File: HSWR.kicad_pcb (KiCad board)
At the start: 4 copper layers, 152 x 139 mm, 150 parts, among them IC1 B1212S-2W, IC2 JW5052C, IC3 JW5052C, IC4 ADUM3054, IC5 ADuM4160, J1 USB_B, J2 IO, J3 B+, J4 B-, J5 U, J6 V, J7 W, J8 SWD, Q1 IXFK300N20X3, Q2 IXFK300N20X3, Q3 IXFK300N20X3, Q4 IXFK300N20X3, Q5 IXFK300N20X3, Q6 IXFK300N20X3, U1 ACS781xLRTR-150B, U2 ACS781xLRTR-150B, U3 ACS781xLRTR-150B, U4 STM32F405RGTx, U5 IRS2186, U6 IRS2186, U7 IRS2186, U8 AP1117-50, Y1 8MHz

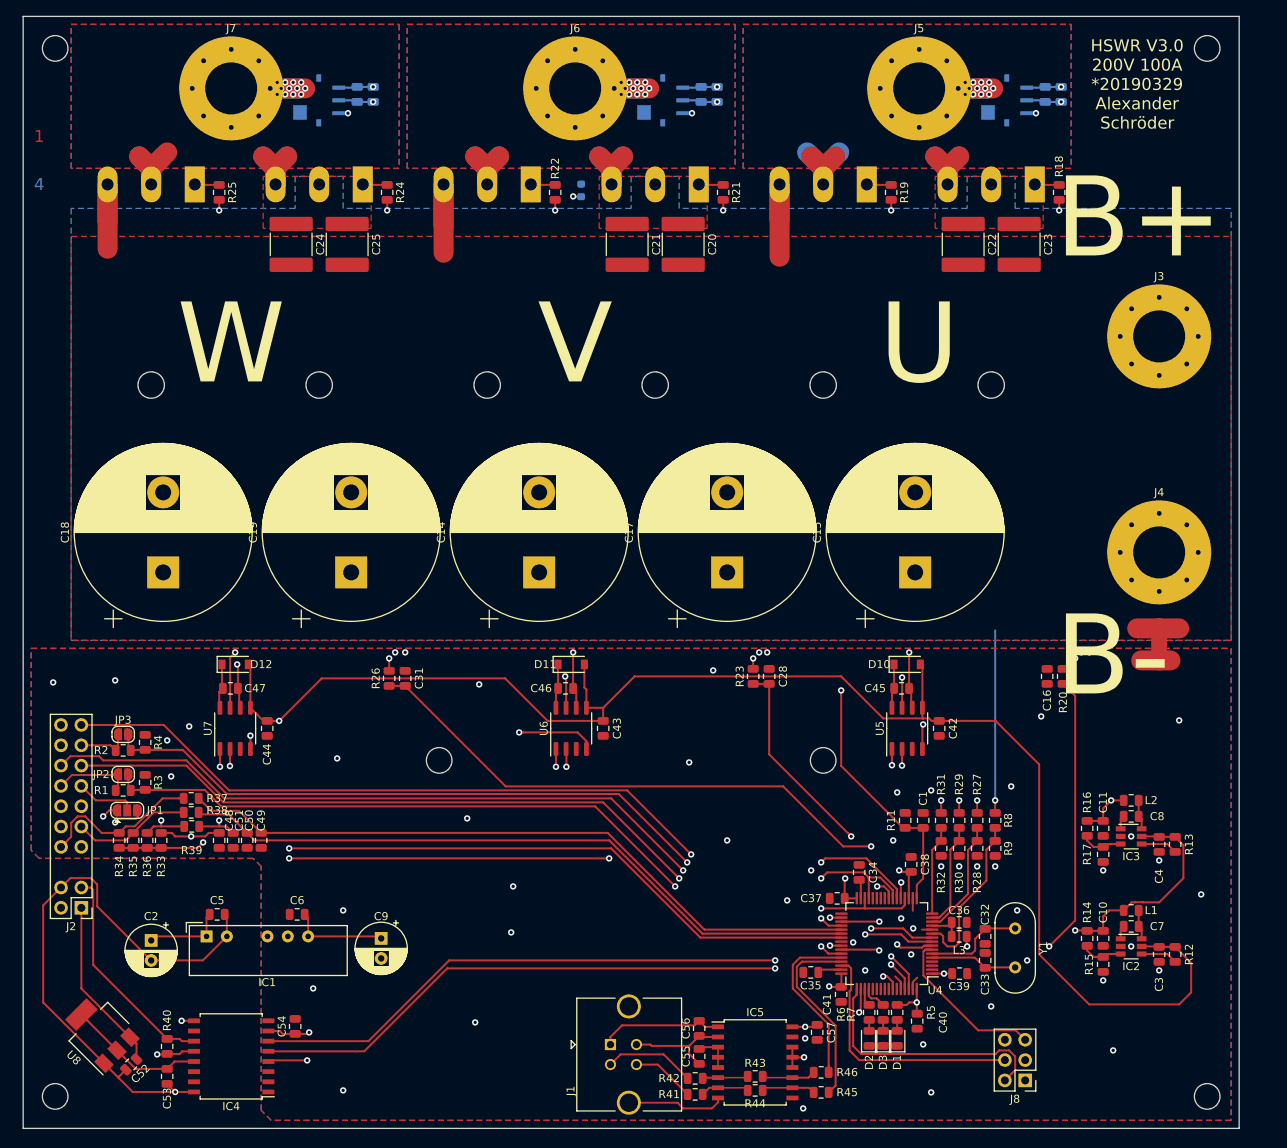
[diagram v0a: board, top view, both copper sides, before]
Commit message: - reworked IO section -> now fully isolated - added fan output - sensor IO is now differential - exposed differential UART interface - fan pin not defined yet!
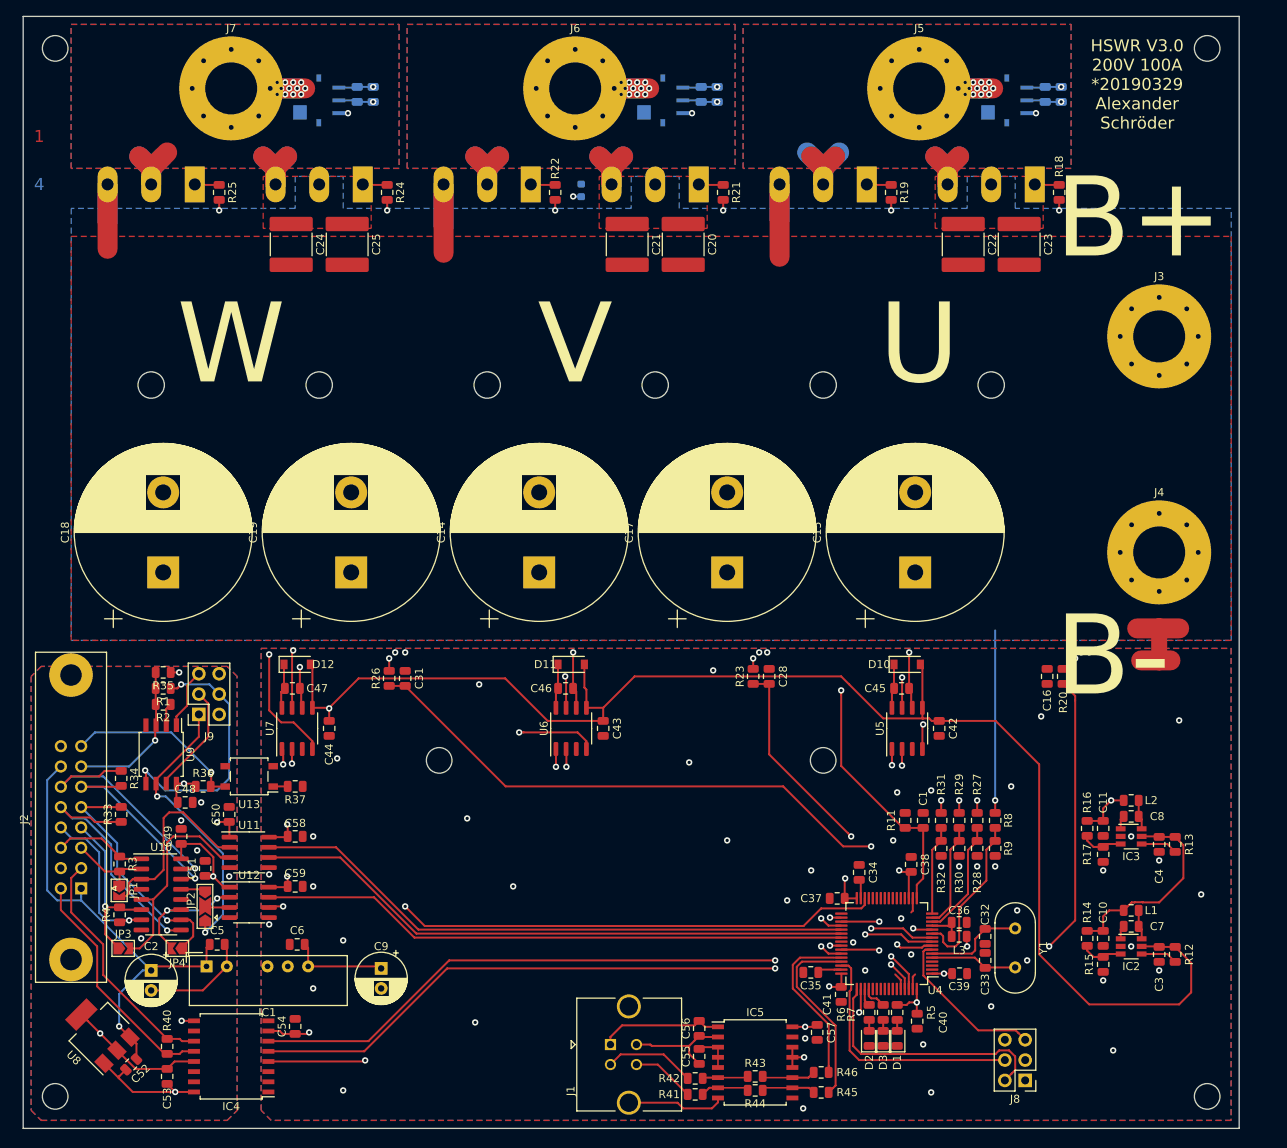
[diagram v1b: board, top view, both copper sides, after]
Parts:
- removed R38, R39: 10k, Resistor_SMD:R_0805_2012Metric
- added C58: 100n, Capacitor_SMD:C_0805_2012Metric, F.Cu at (101.0, 126.5)
- added C59: 100n, Capacitor_SMD:C_0805_2012Metric, F.Cu at (101.0, 132.8)
- added J9: AVR-ISP-6, Connector_PinSocket_2.54mm:PinSocket_2x03_P2.54mm_Vertical, F.Cu at (89.0, 111.2)
- added JP4: H3, Jumper:SolderJumper-2_P1.3mm_Open_TrianglePad1.0x1.5mm, F.Cu at (86.3, 140.5)
- added U10: AM26LV32xD, Package_SO:SOIC-16_3.9x9.9mm_P1.27mm, F.Cu at (84.2, 133.8)
- added U11: ADuM120N, Package_SO:SOIC-8_3.9x4.9mm_P1.27mm, F.Cu at (95.2, 128.5)
- added U12: ADuM120N, Package_SO:SOIC-8_3.9x4.9mm_P1.27mm, F.Cu at (95.2, 134.8)
- added U13: SFH617A-1, Package_SO:SO-4_4.4x4.3mm_P2.54mm, F.Cu at (95.2, 119.0)
- added U9: ATtiny13A-SU, Package_SO:SOIJ-8_5.3x5.3mm_P1.27mm, F.Cu at (84.2, 116.2)
- C48, C49, C50, C51: value 4n7 -> 100n
- J2: footprint Auktora:PinHeader_2x10_P2.54mm_Vertical -> Connector_IDC:IDC-Header_2x08_P2.54mm_Vertical_Lock
- JP1: value 5V/3V3 -> H1; footprint Jumper:SolderJumper-3_P1.3mm_Open_RoundedPad1.0x1.5mm -> Jumper:SolderJumper-2_P1.3mm_Open_TrianglePad1.0x1.5mm
- JP2: value opt. -> UART; footprint Jumper:SolderJumper-2_P1.3mm_Open_RoundedPad1.0x1.5mm -> Jumper:SolderJumper-3_P2.0mm_Open_TrianglePad1.0x1.5mm
- JP3: value opt. -> H2; footprint Jumper:SolderJumper-2_P1.3mm_Open_RoundedPad1.0x1.5mm -> Jumper:SolderJumper-2_P1.3mm_Open_TrianglePad1.0x1.5mm
- R1: value 1k -> 100R
- R3, R4: value 1k5 -> 120R
- R33: value 10k -> 120R
- R34: value 2k2 -> 120R
- R35: value 2k2 -> 10k
- R36: value 2k2 -> 1k
- R37: value 10k -> 100R
- moved JP3 26.8 mm to (79.5, 140.5)
- moved R4 21.8 mm to (79.0, 136.3), turned to 90 degrees
- moved R35 21.3 mm to (84.5, 106.0), turned to 180 degrees
- moved JP2 19.4 mm to (89.8, 135.2), turned to 90 degrees
- moved R1 13.7 mm to (84.5, 108.0)
- moved R37 13.1 mm to (101.0, 120.2), turned to 180 degrees
- moved R3 10.7 mm to (79.0, 129.9)
- moved JP1 10.0 mm to (79.0, 133.2), turned to 270 degrees
- moved C49 10.0 mm to (86.8, 126.5), turned to 90 degrees
- moved R36 9.72 mm to (89.5, 120.2), turned to 0 degrees
- moved R34 7.75 mm to (79.2, 119.2)
- moved C44 7.75 mm to (105.2, 113.0)
- moved C47 7.75 mm to (100.7, 108.0)
- moved D12 7.75 mm to (101.2, 105.0)
- moved U7 7.75 mm to (101.2, 113.0)
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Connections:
- C48 pad 1: /Filters/TEMP_IN -> +5VA
- C48 pad 2: GND -> Earth
- C49 pad 1: /Filters/HALL3_OUT -> +5VA
- C49 pad 2: GND -> Earth
- C50 pad 1: /Filters/HALL2_OUT -> +5VA
- C50 pad 2: GND -> Earth
- C51 pad 1: /Filters/HALL1_OUT -> +5VA
- C51 pad 2: GND -> Earth
- C53 pad 1: Net-(C53-Pad1) -> +5VA
- IC4 pad 10: Net-(IC4-Pad10) -> (no net)
- IC4 pad 13: Net-(C53-Pad1) -> +5VA
- J2 pad 10: /Filters/HALL1_IN -> /iso IO/Hall_3B
- J2 pad 11: /Filters/TEMP_IN -> /iso IO/UART_A
- J2 pad 12: GND -> /iso IO/UART_B
- J2 pad 13: Net-(J2-Pad13) -> /iso IO/M_Temp
- J2 pad 14: Net-(J2-Pad14) -> +12VA
- J2 pad 15: /MCU/RX_SDA_NSS -> /iso IO/Fan_Out
- J2 pad 16: /MCU/TX_SCL_MOSI -> Earth
- J2 pad 7: +5V -> /iso IO/Hall_2A
- J2 pad 8: /Filters/HALL3_IN -> /iso IO/Hall_2B
- J2 pad 9: /Filters/HALL2_IN -> /iso IO/Hall_3A
- J8 pad 6: Net-(J8-Pad6) -> (no net)
- JP1 pad 1: +3V3 -> /iso IO/Hall_1A
- JP1 pad 2: Net-(J2-Pad13) -> Net-(JP1-Pad2)
- JP2 pad 1: Net-(J2-Pad14) -> Net-(J9-Pad1)
- JP2 pad 2: /MCU/SCK_ADC_EXT -> Net-(JP2-Pad2)
- JP3 pad 1: Net-(J2-Pad17) -> /iso IO/Hall_2A
- JP3 pad 2: /MCU/MISO_ADC_EXT2 -> Net-(JP3-Pad2)
- R1 pad 1: /MCU/SCK_ADC_EXT -> Net-(J9-Pad4)
- R1 pad 2: Net-(J2-Pad14) -> /iso IO/M_Temp
- R2 pad 1: /MCU/MISO_ADC_EXT2 -> Net-(R2-Pad1)
- R2 pad 2: Net-(J2-Pad17) -> /iso IO/M_Temp
- R3 pad 1: GND -> /iso IO/Hall_1B
- R3 pad 2: /MCU/SCK_ADC_EXT -> /iso IO/Hall_1A
- R33 pad 1: /Filters/TEMP_IN -> /iso IO/Hall_3B
- R33 pad 2: +3V3 -> /iso IO/Hall_3A
- R34 pad 1: /Filters/HALL3_IN -> /iso IO/UART_B
- R34 pad 2: +3V3 -> /iso IO/UART_A
- R35 pad 1: /Filters/HALL2_IN -> +5VA
- R35 pad 2: +3V3 -> /iso IO/M_Temp
- R36 pad 1: /Filters/HALL1_IN -> +5VA
- R36 pad 2: +3V3 -> /iso IO/Fan_Out
- R37 pad 1: /Filters/HALL3_IN -> (no net)
- R37 pad 2: /Filters/HALL3_OUT -> Net-(R37-Pad2)
- R4 pad 1: GND -> /iso IO/Hall_2B
- R4 pad 2: /MCU/MISO_ADC_EXT2 -> /iso IO/Hall_2A
- U1 pad 4: Net-(U1-Pad4) -> (no net)
- U1 pad 7: Net-(U1-Pad7) -> (no net)
- U2 pad 4: Net-(U2-Pad4) -> (no net)
- U2 pad 7: Net-(U2-Pad7) -> (no net)
- U3 pad 4: Net-(U3-Pad4) -> (no net)
- U3 pad 7: Net-(U3-Pad7) -> (no net)
- U4 pad 2: Net-(U4-Pad2) -> (no net)
- U4 pad 20: /MCU/RX_SDA_NSS -> (no net)
- U4 pad 21: /MCU/SCK_ADC_EXT -> (no net)
- U4 pad 22: /MCU/MISO_ADC_EXT2 -> (no net)
- U4 pad 23: /MCU/TX_SCL_MOSI -> (no net)
- U4 pad 24: /Filters/TEMP_IN -> (no net)
- U4 pad 25: Net-(U4-Pad25) -> (no net)
- U4 pad 26: Net-(U4-Pad26) -> (no net)
- U4 pad 27: Net-(U4-Pad27) -> (no net)
- U4 pad 28: Net-(U4-Pad28) -> (no net)
- U4 pad 29: /MCU/TX_SCL_MOSI -> (no net)
- U4 pad 3: Net-(U4-Pad3) -> (no net)
- U4 pad 30: /MCU/RX_SDA_NSS -> /iso IO/UART
- U4 pad 33: Net-(U4-Pad33) -> (no net)
- U4 pad 37: /Filters/HALL3_OUT -> /MCU/HALL_1
- U4 pad 38: /Filters/HALL2_OUT -> /MCU/HALL_2
- U4 pad 39: /Filters/HALL1_OUT -> /MCU/HALL_3
- U4 pad 4: Net-(U4-Pad4) -> (no net)
- U4 pad 40: Net-(U4-Pad40) -> (no net)
- U4 pad 53: Net-(U4-Pad53) -> (no net)
- U4 pad 54: Net-(U4-Pad54) -> (no net)
- U4 pad 55: Net-(U4-Pad55) -> (no net)
- U4 pad 56: Net-(U4-Pad56) -> (no net)
- U4 pad 57: Net-(U4-Pad57) -> (no net)
- U4 pad 58: /MCU/SERVO -> (no net)
- U4 pad 59: Net-(U4-Pad59) -> (no net)
- U8 pad 2: Net-(C53-Pad1) -> +5VA
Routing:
- net +5V: track 177.0 -> 25.6 mm, vias 2 -> 0
- net /MCU/SERVO: track 122.3 -> 0.00 mm, vias 2 -> 0
- net /Filters/TEMP_IN: track 117.5 -> 0.00 mm, vias 4 -> 0
- net /MCU/TX_SCL_MOSI: track 115.6 -> 0.00 mm, vias 2 -> 0
- net /MCU/RX_SDA_NSS: track 112.7 -> 0.00 mm, vias 2 -> 0
- net /MCU/MISO_ADC_EXT2: track 106.7 -> 0.00 mm, vias 2 -> 0
- net /MCU/SCK_ADC_EXT: track 106.3 -> 0.00 mm, vias 2 -> 0
- net /Filters/HALL1_OUT: track 89.2 -> 0.00 mm, vias 2 -> 0
- net /Filters/HALL3_OUT: track 87.1 -> 0.00 mm
- net /Filters/HALL2_OUT: track 86.6 -> 0.00 mm
- net /iso IO/UART: track 0.00 -> 77.5 mm, vias 0 -> 2
- net /MCU/HALL_1: track 0.00 -> 75.8 mm
- net /MCU/HALL_2: track 0.00 -> 75.5 mm
- net /MCU/HALL_3: track 0.00 -> 73.6 mm
- net Earth: track 83.5 -> 39.9 mm, vias 2 -> 7
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- added copper zone on GND, net +12VA
- added copper zone on Power1, net +5VA
- added copper zone on B.Cu, net Earth
- added copper zone on F.Cu, net Earth

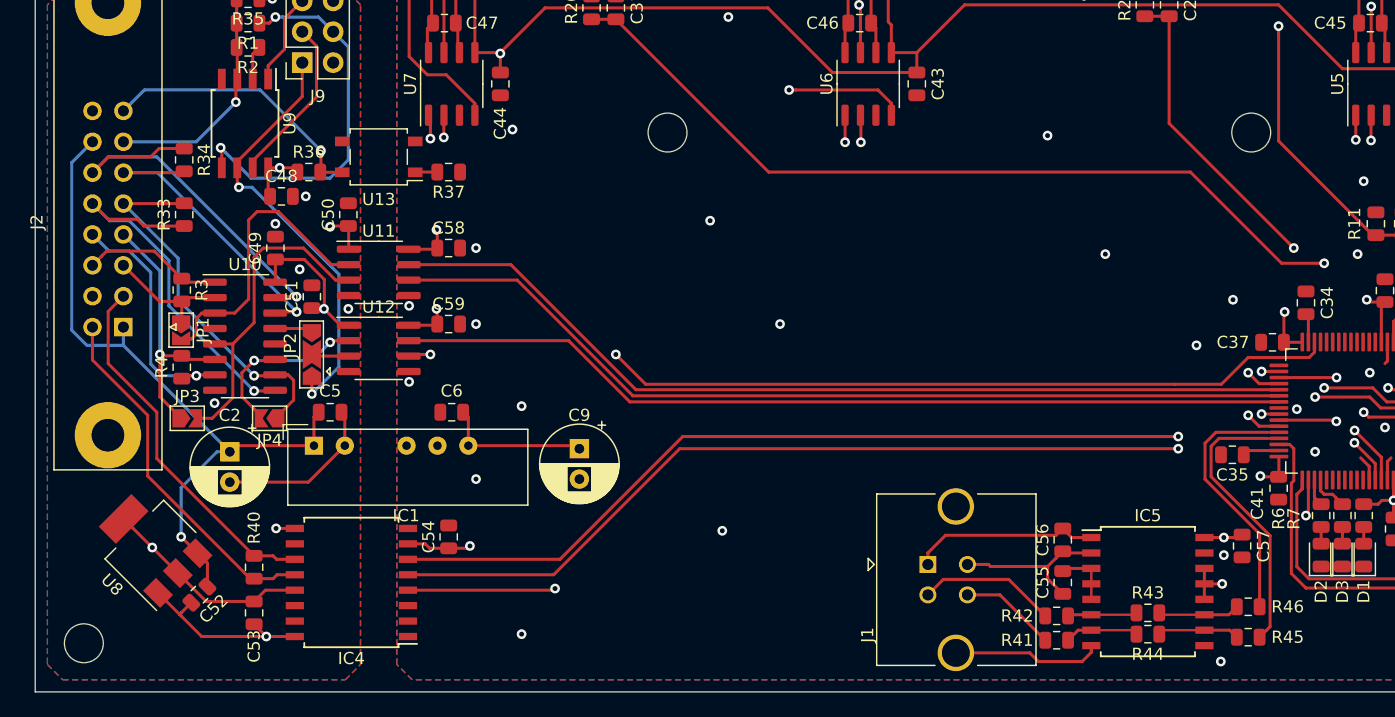
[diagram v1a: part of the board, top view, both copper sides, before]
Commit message: - added high power capabilities to fan output - moved CAN isolator - connected fan output to PB10 (TIM2_CH3)
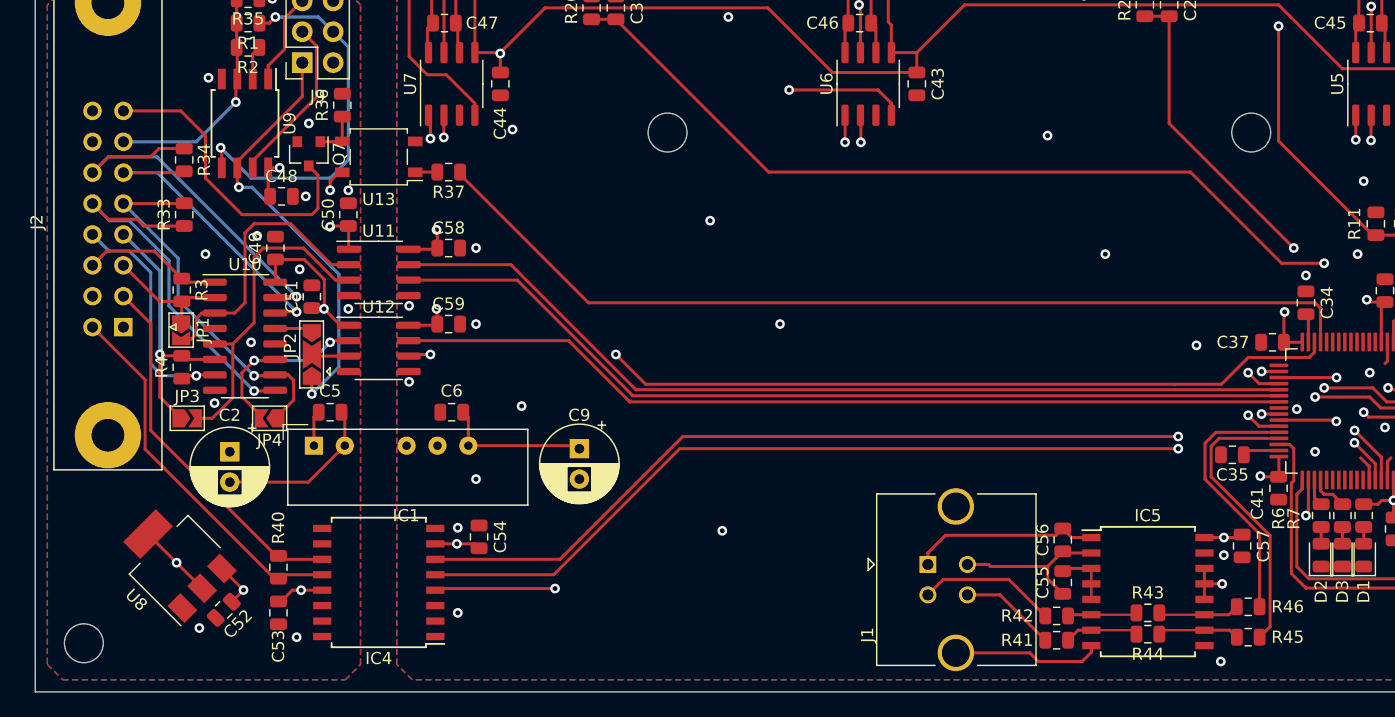
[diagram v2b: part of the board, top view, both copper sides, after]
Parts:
- added Q7: Q_NMOS_GSD, Package_TO_SOT_SMD:SOT-23, F.Cu at (89.5, 118.8)
- U13: value SFH617A-1 -> PC355
- moved R36 6.15 mm to (92.2, 114.8), turned to 90 degrees
- moved C54 2.50 mm to (103.5, 150.2)
- moved C52 2.36 mm to (82.5, 156.2)
- moved U8 2.36 mm to (78.5, 152.2)
- moved IC4 2.25 mm to (95.2, 154.0)
- moved C53 2.00 mm to (87.0, 156.5)
- moved R40 2.00 mm to (87.0, 152.8)
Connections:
- IC4 pad 10: (no net) -> Net-(IC4-Pad10)
- J8 pad 6: (no net) -> Net-(J8-Pad6)
- R36 pad 1: +5VA -> Net-(Q7-Pad1)
- R36 pad 2: /iso IO/Fan_Out -> Earth
- R37 pad 1: (no net) -> /MCU/Fan_CPU
- U1 pad 4: (no net) -> Net-(U1-Pad4)
- U1 pad 7: (no net) -> Net-(U1-Pad7)
- U10 pad 12: (no net) -> Earth
- U10 pad 4: (no net) -> Net-(U10-Pad4)
- U13 pad 3: Earth -> Net-(Q7-Pad1)
- U13 pad 4: /iso IO/Fan_Out -> +12VA
- U2 pad 4: (no net) -> Net-(U2-Pad4)
- U2 pad 7: (no net) -> Net-(U2-Pad7)
- U3 pad 4: (no net) -> Net-(U3-Pad4)
- U3 pad 7: (no net) -> Net-(U3-Pad7)
- U4 pad 2: (no net) -> Net-(U4-Pad2)
- U4 pad 20: (no net) -> Net-(U4-Pad20)
- U4 pad 21: (no net) -> Net-(U4-Pad21)
- U4 pad 22: (no net) -> Net-(U4-Pad22)
- U4 pad 23: (no net) -> Net-(U4-Pad23)
- U4 pad 24: (no net) -> Net-(U4-Pad24)
- U4 pad 25: (no net) -> Net-(U4-Pad25)
- U4 pad 26: (no net) -> Net-(U4-Pad26)
- U4 pad 27: (no net) -> Net-(U4-Pad27)
- U4 pad 28: (no net) -> Net-(U4-Pad28)
- U4 pad 29: (no net) -> /MCU/Fan_CPU
- U4 pad 3: (no net) -> Net-(U4-Pad3)
- U4 pad 33: (no net) -> Net-(U4-Pad33)
- U4 pad 4: (no net) -> Net-(U4-Pad4)
- U4 pad 40: (no net) -> Net-(U4-Pad40)
- U4 pad 53: (no net) -> Net-(U4-Pad53)
- U4 pad 54: (no net) -> Net-(U4-Pad54)
- U4 pad 55: (no net) -> Net-(U4-Pad55)
- U4 pad 56: (no net) -> Net-(U4-Pad56)
- U4 pad 57: (no net) -> Net-(U4-Pad57)
- U4 pad 58: (no net) -> Net-(U4-Pad58)
- U4 pad 59: (no net) -> Net-(U4-Pad59)
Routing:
- net /MCU/Fan_CPU: track 0.00 -> 78.3 mm
- net +12VA: track 59.1 -> 8.83 mm, vias 1 -> 2
- net Earth: track 39.9 -> 13.6 mm, vias 7 -> 12
- net +5VA: track 39.4 -> 30.8 mm, vias 5 -> 6
- net Net-(Q7-Pad1): track 0.00 -> 3.85 mm
- net /iso IO/Fan_Out: track 22.6 -> 25.6 mm, vias 1 -> 0
- net /CAN bus transceiver/CAN_TX: track 87.2 -> 85.0 mm
- net /CAN bus transceiver/CAN_RX: track 86.5 -> 84.3 mm
- net /MCU/CAN_VSS_SENSE: track 83.4 -> 81.3 mm
- net +3V3: track 283.9 -> 282.3 mm
- net Net-(JP1-Pad2): track 24.5 -> 23.2 mm
- net /CAN bus transceiver/CANH: track 29.9 -> 30.9 mm
- net GND: vias 53 -> 54
